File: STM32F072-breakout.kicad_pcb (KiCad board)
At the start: 2 copper layers, 31 parts, among them J1 USB_B_Micro, J2 Conn_01x04_Pin, J3 Conn_01x30_Pin, J4 Conn_01x30_Pin, SW1 SW_SPST, U1 STM32F072RBTx, U2 XC6206P332MR, Y1 8MHz

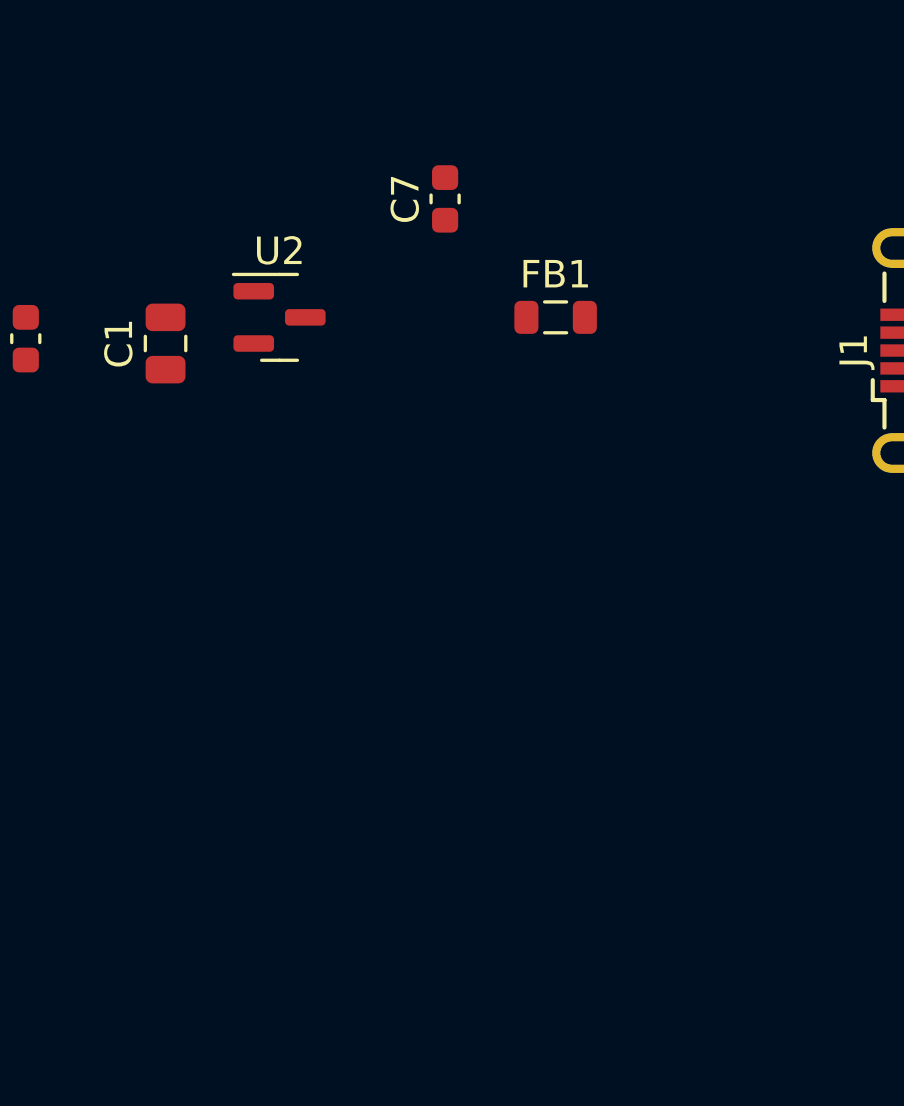
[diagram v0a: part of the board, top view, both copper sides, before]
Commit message: use ams1117 for 3.3V
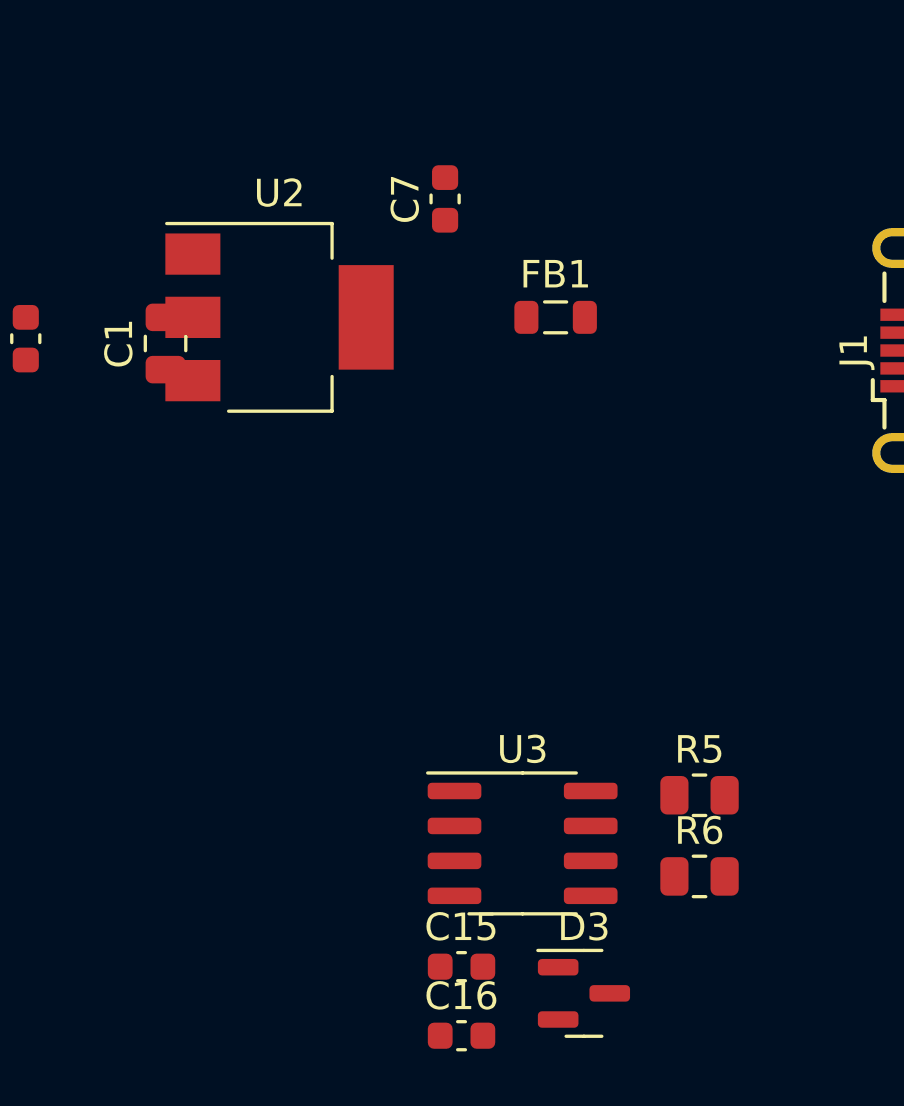
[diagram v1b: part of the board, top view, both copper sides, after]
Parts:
- added C15: 20pf, Capacitor_SMD:C_0603_1608Metric, F.Cu at (188.6, 79.5)
- added C16: 100nf, Capacitor_SMD:C_0603_1608Metric, F.Cu at (188.6, 82.0)
- added D3: BAT54C, Package_TO_SOT_SMD:SOT-23, F.Cu at (193.0, 80.5)
- added R5: R, Resistor_SMD:R_0805_2012Metric, F.Cu at (197.2, 73.2)
- added R6: 60, Resistor_SMD:R_0805_2012Metric, F.Cu at (197.2, 76.2)
- added U3: MCP2551-I-SN, Package_SO:SOIC-8_3.9x4.9mm_P1.27mm, F.Cu at (190.8, 75.0)
- C7, C8: value 1u -> 10u
- U2: value XC6206P332MR -> AMS1117-3.3; footprint Package_TO_SOT_SMD:SOT-23 -> Package_TO_SOT_SMD:SOT-223-3_TabPin2

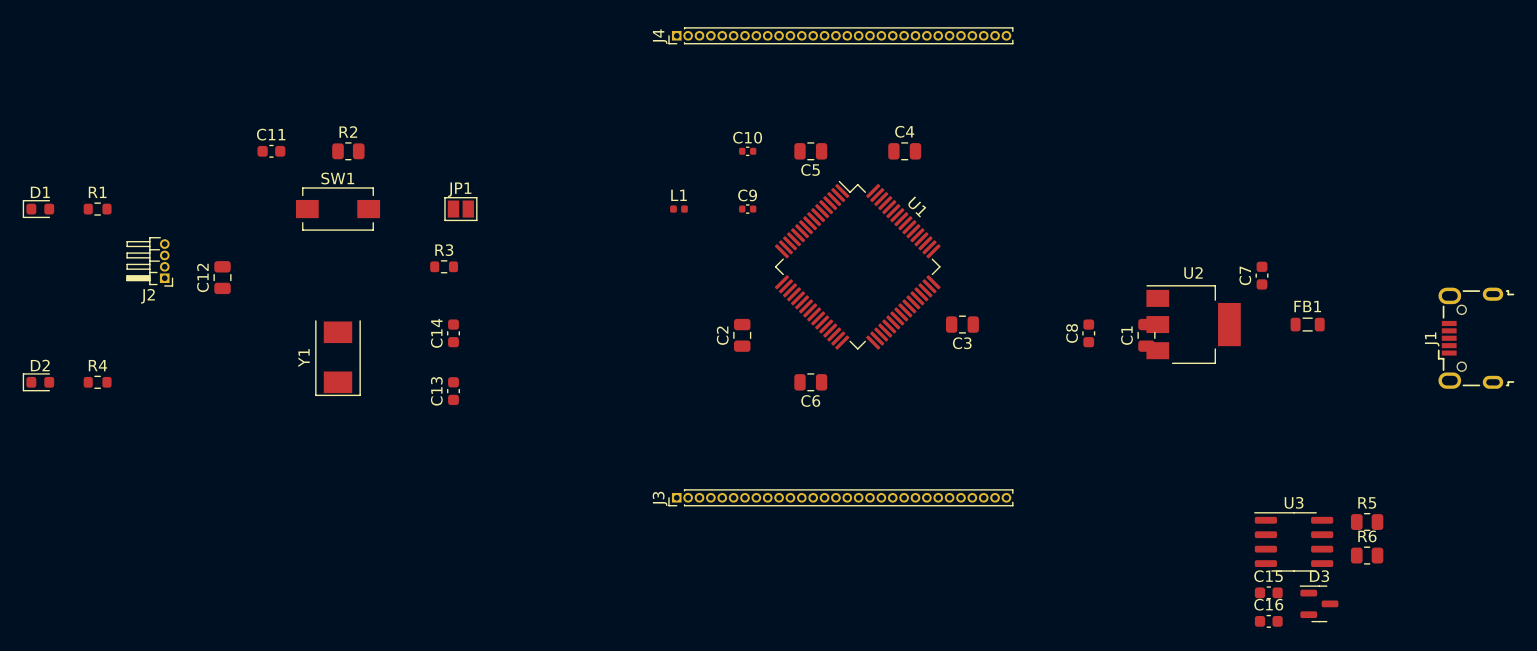
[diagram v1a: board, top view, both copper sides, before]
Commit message: fix missing CAN connection
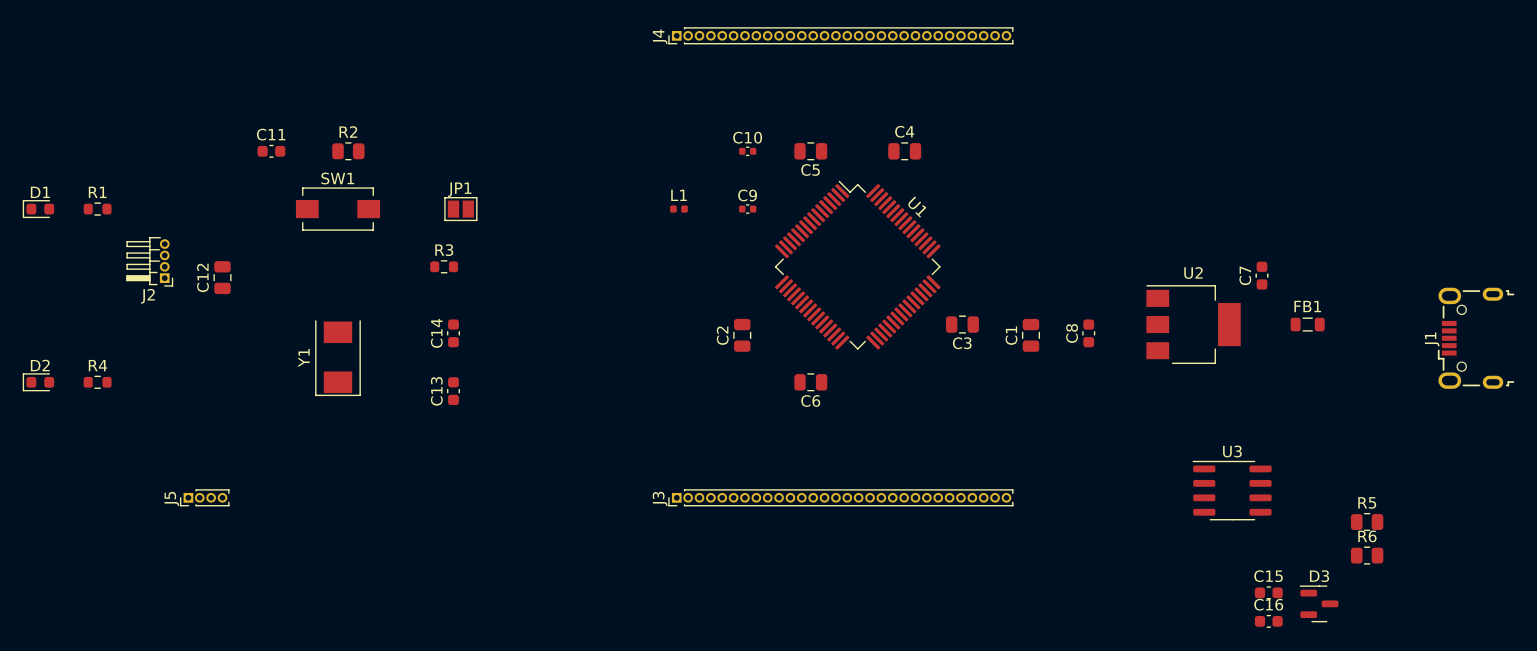
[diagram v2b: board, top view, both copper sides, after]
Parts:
- added J5: Conn_01x04_Pin, Connector_PinHeader_1.00mm:PinHeader_1x04_P1.00mm_Vertical, F.Cu at (93.5, 71.1)
- moved C1 10.2 mm to (167.6, 56.8)
- moved U3 7.06 mm to (185.4, 70.5)
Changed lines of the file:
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@@
   )
   (footprint "Package_SO:SOIC-8_3.9x4.9mm_P1.27mm" (layer "F.Cu")
-    (at 190.7775 75)
+    (at 185.355 70.485)
     (descr "SOIC, 8 Pin (JEDEC MS-012AA, https://www.analog.com/media/en/package-pcb-resources/package/pkg_pdf/soic_narrow-r/r_8.pdf), generated with kicad-footprint-generator ipc_gullwing_generator.py")
     (tags "SOIC SO")
@@
       (net 64 "CAN_2") (pinfunction "RXD") (pintype "output"))
     (pad "5" smd roundrect (at 2.475 1.905) (size 1.95 0.6) (layers "F.Cu" "F.Paste" "F.Mask") (roundrect_rratio 0.25)
-      (net 71 "unconnected-(U3-Vref-Pad5)") (pinfunction "Vref") (pintype "power_out"))
+      (net 71 "unconnected-(U3-Vref-Pad5)") (pinfunction "Vref") (pintype "power_out+no_connect"))
     (pad "6" smd roundrect (at 2.475 0.635) (size 1.95 0.6) (layers "F.Cu" "F.Paste" "F.Mask") (roundrect_rratio 0.25)
       (net 69 "CAN-") (pinfunction "CANL") (pintype "bidirectional"))
@@
       (net 2 "GND") (pintype "passive"))
     (model "${KICAD6_3DMODEL_DIR}/Capacitor_SMD.3dshapes/C_0805_2012Metric.wrl"
+      (offset (xyz 0 0 0))
+      (scale (xyz 1 1 1))
+      (rotate (xyz 0 0 0))
+    )
+  )
+  (footprint "Connector_PinHeader_1.00mm:PinHeader_1x04_P1.00mm_Vertical" (layer "F.Cu")
+    (at 93.52 71.12 90)
+    (descr "Through hole straight pin header, 1x04, 1.00mm pitch, single row")
+    (tags "Through hole pin header THT 1x04 1.00mm single row")
+    (property "Sheetfile" "STM32F072-breakout.kicad_sch")
+    (property "Sheetname" "")
+    (property "ki_description" "Generic connector, single row, 01x04, script generated")
+    (property "ki_keywords" "connector")
+    (attr through_hole)
+    (fp_text reference "J5" (at 0 -1.56 90) (layer "F.SilkS")
+        (effects (font (size 1 1) (thickness 0.15)))
+    )
+    (fp_text value "Conn_01x04_Pin" (at 0 4.56 90) (layer "F.Fab")
+        (effects (font (size 1 1) (thickness 0.15)))
+    )
+    (fp_text user "${REFERENCE}" (at 0 1.5) (layer "F.Fab")
+        (effects (font (size 0.76 0.76) (thickness 0.114)))
+    )
+    (fp_line (start -0.695 -0.685) (end 0 -0.685)
+      (stroke (width 0.12) (type solid)) (layer "F.SilkS"))
+    (fp_line (start -0.695 0) (end -0.695 -0.685)
+      (stroke (width 0.12) (type solid)) (layer "F.SilkS"))
+    (fp_line (start -0.695 0.685) (end -0.695 3.56)
+      (stroke (width 0.12) (type solid)) (layer "F.SilkS"))
+    (fp_line (start -0.695 0.685) (end -0.608276 0.685)
+      (stroke (width 0.12) (type solid)) (layer "F.SilkS"))
+    (fp_line (start -0.695 3.56) (end -0.394493 3.56)
+      (stroke (width 0.12) (type solid)) (layer "F.SilkS"))
+    (fp_line (start 0.394493 3.56) (end 0.695 3.56)
+      (stroke (width 0.12) (type solid)) (layer "F.SilkS"))
+    (fp_line (start 0.608276 0.685) (end 0.695 0.685)
+      (stroke (width 0.12) (type solid)) (layer "F.SilkS"))
+    (fp_line (start 0.695 0.685) (end 0.695 3.56)
+      (stroke (width 0.12) (type solid)) (layer "F.SilkS"))
+    (fp_line (start -1.15 -1) (end -1.15 4)
+      (stroke (width 0.05) (type solid)) (layer "F.CrtYd"))
+    (fp_line (start -1.15 4) (end 1.15 4)
+      (stroke (width 0.05) (type solid)) (layer "F.CrtYd"))
+    (fp_line (start 1.15 -1) (end -1.15 -1)
+      (stroke (width 0.05) (type solid)) (layer "F.CrtYd"))
+    (fp_line (start 1.15 4) (end 1.15 -1)
+      (stroke (width 0.05) (type solid)) (layer "F.CrtYd"))
+    (fp_line (start -0.635 -0.1825) (end -0.3175 -0.5)
+      (stroke (width 0.1) (type solid)) (layer "F.Fab"))
+    (fp_line (start -0.635 3.5) (end -0.635 -0.1825)
+      (stroke (width 0.1) (type solid)) (layer "F.Fab"))
+    (fp_line (start -0.3175 -0.5) (end 0.635 -0.5)
+      (stroke (width 0.1) (type solid)) (layer "F.Fab"))
+    (fp_line (start 0.635 -0.5) (end 0.635 3.5)
+      (stroke (width 0.1) (type solid)) (layer "F.Fab"))
+    (fp_line (start 0.635 3.5) (end -0.635 3.5)
+      (stroke (width 0.1) (type solid)) (layer "F.Fab"))
+    (pad "1" thru_hole rect (at 0 0 90) (size 0.85 0.85) (drill 0.5) (layers "*.Cu" "*.Mask")
+      (net 66 "Net-(J5-Pin_1)") (pinfunction "Pin_1") (pintype "passive"))
+    (pad "2" thru_hole oval (at 0 1 90) (size 0.85 0.85) (drill 0.5) (layers "*.Cu" "*.Mask")
+      (net 68 "CAN+") (pinfunction "Pin_2") (pintype "passive"))
+    (pad "3" thru_hole oval (at 0 2 90) (size 0.85 0.85) (drill 0.5) (layers "*.Cu" "*.Mask")
+      (net 69 "CAN-") (pinfunction "Pin_3") (pintype "passive"))
+    (pad "4" thru_hole oval (at 0 3 90) (size 0.85 0.85) (drill 0.5) (layers "*.Cu" "*.Mask")
+      (net 2 "GND") (pinfunction "Pin_4") (pintype "passive"))
+    (model "${KICAD6_3DMODEL_DIR}/Connector_PinHeader_1.00mm.3dshapes/PinHeader_1x04_P1.00mm_Vertical.wrl"
       (offset (xyz 0 0 0))
       (scale (xyz 1 1 1))
@@
   )
   (footprint "Capacitor_SMD:C_0805_2012Metric" (layer "F.Cu")
-    (at 177.8 56.83 90)
+    (at 167.64 56.83 90)
     (descr "Capacitor SMD 0805 (2012 Metric), square (rectangular) end terminal, IPC_7351 nominal, (Body size source: IPC-SM-782 page 76, https://www.pcb-3d.com/wordpress/wp-content/uploads/ipc-sm-782a_amendment_1_and_2.pdf, https://docs.google.com/spreadsheets/d/1BsfQQcO9C6DZCsRaXUlFlo91Tg2WpOkGARC1WS5S8t0/edit?usp=sharing), generated with kicad-footprint-generator")
     (tags "capacitor")
